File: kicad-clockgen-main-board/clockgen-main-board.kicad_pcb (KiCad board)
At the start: 2 copper layers, 70 x 64.4 mm, 16 parts, among them J1 CLK0_SMA, J2 CLK1_SMA, J3 Headswitch_SMA, J4 Headswitch_BNC

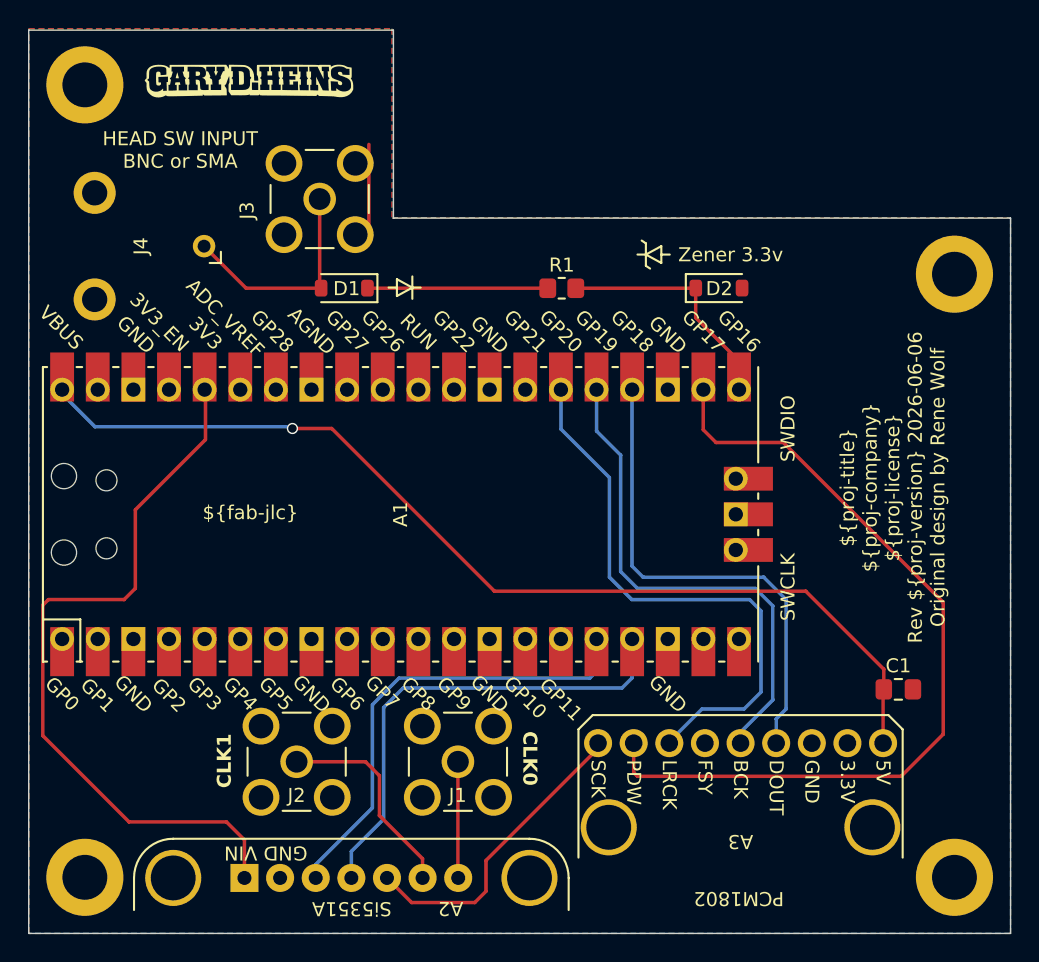
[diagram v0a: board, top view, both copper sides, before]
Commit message: Add board reference variable to project configuration
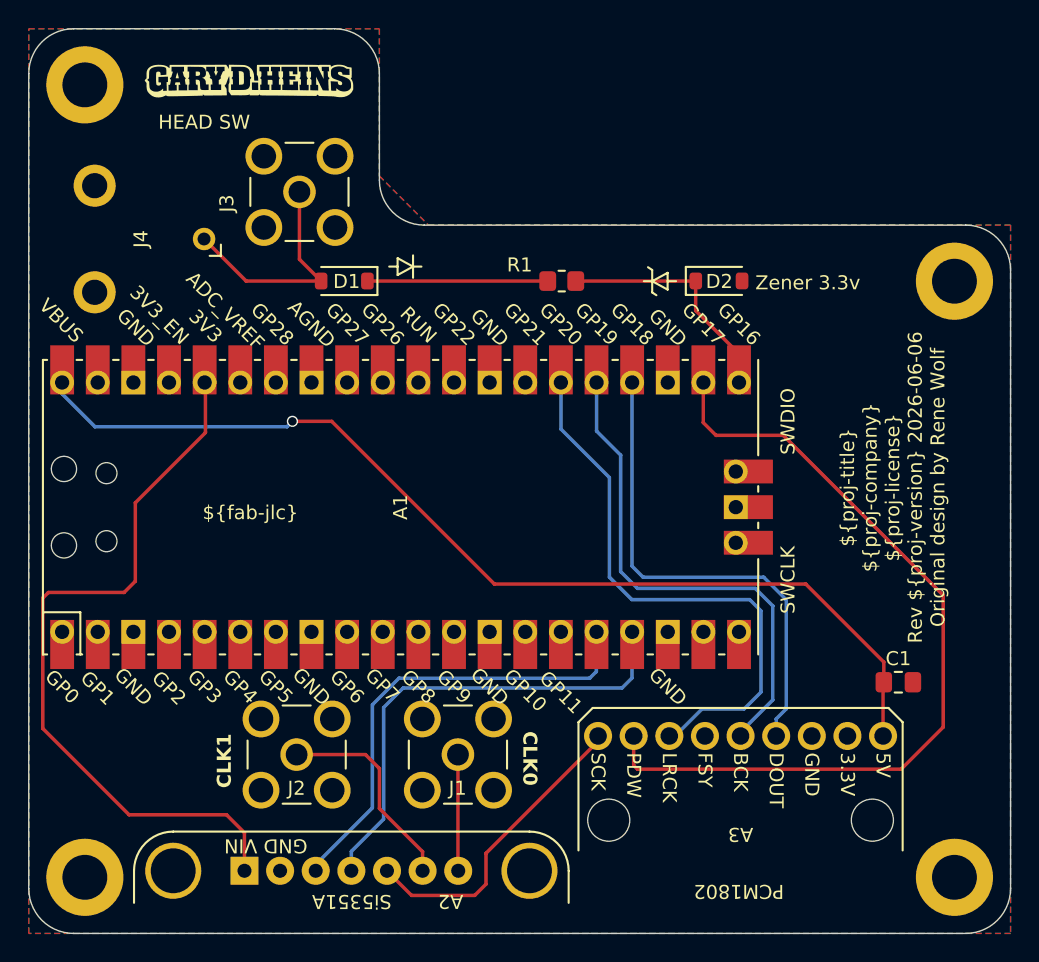
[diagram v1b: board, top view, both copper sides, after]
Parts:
- added ${board-ref}**: Board, PCM_kikit:Board, F.Cu at (98.0, 65.5)
- moved J3 1.53 mm to (117.3, 77.1)
- moved A1 0.51 mm to (124.5, 99.6)
- moved A2 0.51 mm to (121.0, 122.7)
- moved A3 0.51 mm to (148.8, 113.9)
- moved D1 0.51 mm to (120.5, 83.5)
- moved D2 0.51 mm to (147.2, 83.5)
- moved J1 0.51 mm to (128.6, 117.2)
- moved J2 0.51 mm to (117.1, 117.2)
- moved J4 0.51 mm to (110.5, 80.5)
- moved R1 0.51 mm to (136.0, 83.5)
- moved C1 0.51 mm to (160.0, 112.1)
- moved H2 0.50 mm to (164.0, 83.5)
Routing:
- net GND: track 6.80 -> 0.00 mm
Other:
- board size 70 x 64.4 mm -> 70 x 64.5 mm
- board text added: "${board-ref}"
- board text added: "HEAD SW"
- board text removed: "HEAD SW INPUT BNC or SMA"
